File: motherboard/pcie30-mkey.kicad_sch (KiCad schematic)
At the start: 0 parts

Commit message: implemented most features
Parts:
- added C37, C38, C39, C40, C41, C42, C43, C44: 220nF, symbol Device:C_Small
- added C45, C46: 22uF, symbol Device:C_Small
- added C47, C57, C60, C62, C63: 1uF, symbol Device:C_Small
- added C48: 0.1uF, symbol Device:C_Small
- added C49: 100nF, Capacitor_SMD:C_0402_1005Metric, symbol Device:C_Small
- added C50: 10uF, Capacitor_SMD:C_1206_3216Metric, symbol Device:C_Small
- added C51: 1uF, Capacitor_SMD:C_1206_3216Metric, symbol Device:C_Small
- added C52: 22uF, Capacitor_SMD:C_0603_1608Metric, symbol Device:C_Small
- added C53: 8.2nF, Capacitor_SMD:C_0603_1608Metric, symbol Device:C_Small
- added C54: 1nF, Capacitor_SMD:C_0402_1005Metric, symbol Device:C_Small
- added C55: 10pF, Capacitor_SMD:C_0402_1005Metric, symbol Device:C_Small
- added C56, C61: 100nF, symbol Device:C_Small
- added C58, C59: 15pF, symbol Device:C_Small
- added D5: SS54, Diode_SMD:D_SMA, symbol Device:D_Schottky
- added IC1: PI6C557-05BLE, SOP65P640X120-20N:SOP65P640X120-20N, symbol PI6C557-05B:PI6C557-05BLE
- added J15: Bus_M.2_Socket_M, symbol Connector:Bus_M.2_Socket_M
- added L1: 3.3uH, Inductor_SMD:L_Vishay_IHLP-1616, symbol Device:L_Small
- added R63: 10k, Resistor_SMD:R_0402_1005Metric, symbol Device:R_Small
- added R64: 3.3k, Resistor_SMD:R_0402_1005Metric, symbol Device:R_Small
- added R65, R66: 13k, Resistor_SMD:R_0603_1608Metric, symbol Device:R_Small
- added R67: 4.7k, symbol Device:R_Small
- added R68, R69: NC, symbol Device:R_Small
- added R70, R71: 10k, symbol Device:R_Small
- added R72: 470R, symbol Device:R_Small
- added R73: 100R, symbol Device:R_Small
- added R74, R75, R78, R79, R82, R83: 33R, symbol Device:R_Small
- added R76, R77, R80, R81, R84, R85: 49.9R, symbol Device:R_Small
- added U20: TPS54331DR, TPS54331DR:SOIC127P599X175-8N, symbol TPS54331DR:TPS54331DR
- added U21: AP2127K-3.3, Package_TO_SOT_SMD:SOT-23-5, symbol Regulator_Linear:AP2127K-3.3
- added Y1: 25MHz, symbol Device:Crystal_GND24_Small
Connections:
- new net: R65.2, R66.1
- new net: C54.1, R66.2
- new net: C49.2, D5.1 (K), L1.2, U20.8 (PH)
- new net: IC1.8 (OE), R71.2
- new net: C59.1, R73.2, Y1.3
- new net: C38.2, J15.23 (PETn2)
- new net: R63.2, R64.1, U20.5 (VSENSE)
- new net: C39.2, J15.13 (PETp3)
- new net: C49.1, U20.1 (BOOT)
- new net: C53.1, U20.4 (SS)
- new net: C55.1, R65.1, U20.6 (COMP)
- new net: IC1.10 (IREF), R72.2
- new net: C42.2, J15.35 (PETn1)
- new net: C40.2, J15.25 (PETp2)
- new net: IC1.4 (S2), R67.2
- new net: IC1.3 (S1), R68.2
- new net: C43.2, J15.47 (PETn0/SATA-A-)
- new net: C41.2, J15.37 (PETp1)
- new net: C37.2, J15.11 (PETn3)
- new net: IC1.19 (~{CLK0}), R75.1
- new net: IC1.2 (S0), R69.2
- new net: IC1.20 (CLK0), R74.1
- new net: IC1.7 (~{PD}), R70.2
- new net: C44.2, J15.49 (PETp0/SATA-A+)
- new net +3.3V: U21.3 (EN)
- new net +3.3V_PCIE: C45.1, C46.1, C47.1, C48.1, C50.1, C51.1, J15.12 (3.3V), J15.14 (3.3V), J15.16 (3.3V), J15.18 (3.3V), J15.2 (3.3V), J15.4 (3.3V), J15.70 (3.3V), J15.72 (3.3V), J15.74 (3.3V), L1.1, R63.1
- new net +3.3V_PI6C: C56.1, C57.1, C60.1, C61.1, C63.1, IC1.1 (VDDXD), IC1.15 (VDDODA), R70.1, R71.1, U21.5 (VOUT)
- new net +5V: C62.1, U21.1 (VIN)
- new net +5v: C52.1, U20.2 (VIN)
- new net CLK2N: IC1.13 (~{CLK2}), R79.1
- new net CLK2P: IC1.14 (CLK2), R78.1
- new net CLK3N: IC1.11 (~{CLK3}), R83.1
- new net CLK3P: IC1.12 (CLK3), R82.1
- new net EN: U20.3 (EN)
- new net GND: C45.2, C46.2, C47.2, C48.2, C50.2, C51.2, C52.2, C53.2, C54.2, C55.2, C56.2, C57.2, C58.2, C59.2, C60.2, C61.2, C62.2, C63.2, D5.2 (A), IC1.16 (GNDODA), IC1.9 (GNDXD), J15.1 (GND), J15.15 (GND), J15.21 (GND), J15.27 (GND), J15.3 (GND), J15.33 (GND), J15.39 (GND), J15.45 (GND), J15.51 (GND), J15.57 (GND), J15.71 (GND), J15.73 (GND), J15.75 (GND), J15.9 (GND), R64.2, R67.1, R68.1, R69.1, R72.1, R76.1, R77.1, R80.1, R81.1, R84.1, R85.1, U20.7 (GND), U21.2 (GND), Y1.2, Y1.4
- new net GPIO4_B4/PCIE30X4_CLKREQn_M1_L: J15.52 (~{CLKREQ})
- new net GPIO4_B5/PCIE30X4_WAKEn_M1_L: J15.54 (~{PEWAKE})
- new net GPIO4_B6/PCIE30X4_PERSTn_M1_L: J15.50 (~{PERST})
- new net PCIE30_PORT0_REFCLKN_IN: R83.2, R85.2
- new net PCIE30_PORT0_REFCLKP_IN: R82.2, R84.2
- new net PCIE30_PORT0_RX0N: J15.41 (PERn0/SATA-B+)
- new net PCIE30_PORT0_RX0P: J15.43 (PERp0/SATA-B-)
- new net PCIE30_PORT0_RX1N: J15.29 (PERn1)
- new net PCIE30_PORT0_RX1P: J15.31 (PERp1)
- new net PCIE30_PORT0_TX0N: C43.1
- new net PCIE30_PORT0_TX0P: C44.1
- new net PCIE30_PORT0_TX1N: C42.1
- new net PCIE30_PORT0_TX1P: C41.1
- new net PCIE30_PORT1_RX2N: J15.17 (PERn2)
- new net PCIE30_PORT1_RX2P: J15.19 (PERp2)
- new net PCIE30_PORT1_RX3N: J15.5 (PERn3)
- new net PCIE30_PORT1_RX3P: J15.7 (PERp3)
- new net PCIE30_PORT1_TX2N: C38.1
- new net PCIE30_PORT1_TX2P: C40.1
- new net PCIE30_PORT1_TX3N: C37.1
- new net PCIE30_PORT1_TX3P: C39.1
- new net PCIE30_REFCLKN_SLOT: J15.53 (REFCLKn)
- new net PCIE30_REFCLKP_SLOT: J15.55 (REFCLKp)
- new net PCIE30_REFCLK_A_N: R75.2, R77.2
- new net PCIE30_REFCLK_A_P: R74.2, R76.2
- new net PCIE30_REFCLK_B_N: R79.2, R81.2
- new net PCIE30_REFCLK_B_P: R78.2, R80.2
- new net X1: C58.1, IC1.5 (X1), Y1.1
- new net X2: IC1.6 (X2), R73.1
- no-connect marks 0 -> 6
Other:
- note added: "internal pull up"

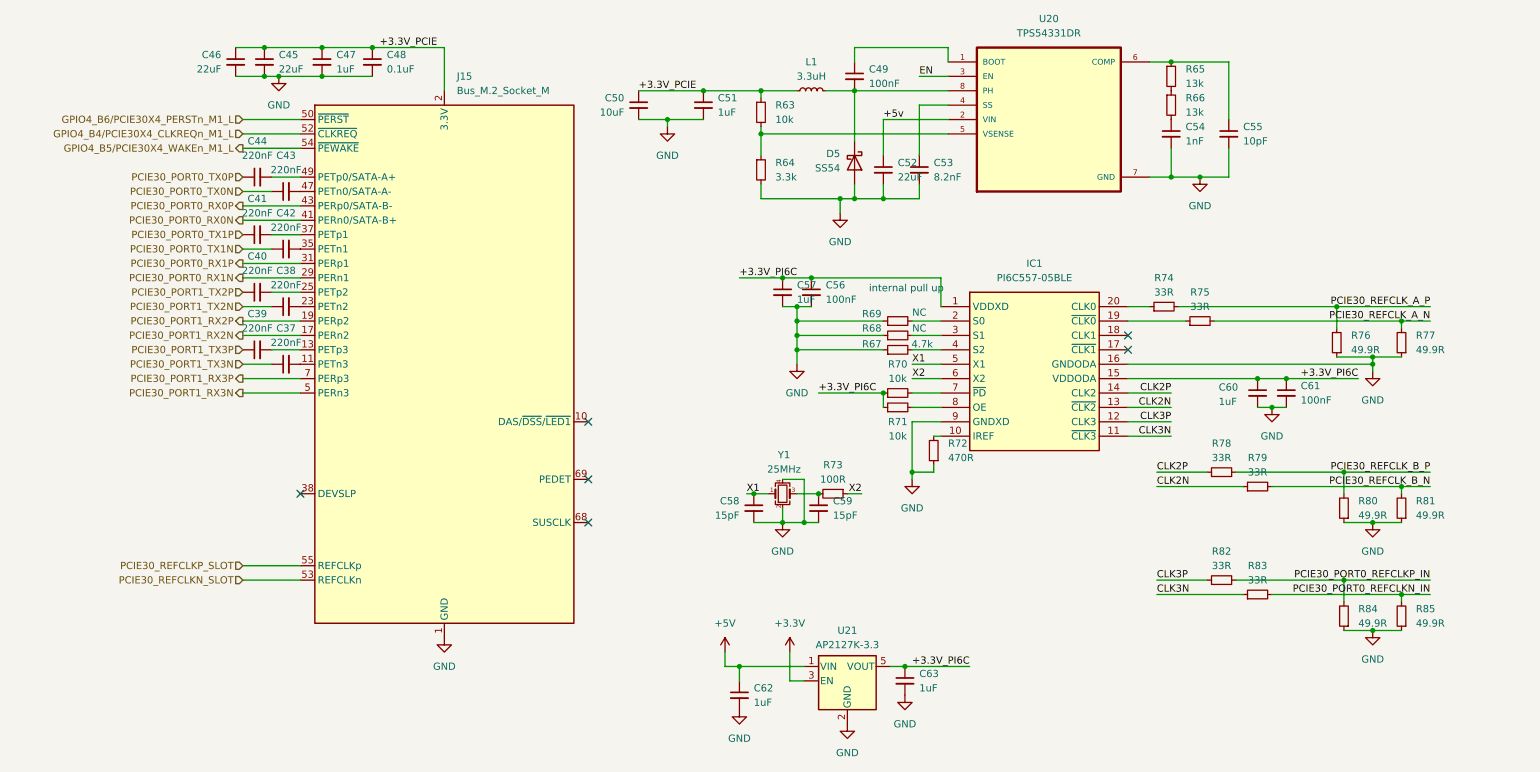
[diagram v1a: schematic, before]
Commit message: synchronizing hierarchical pins
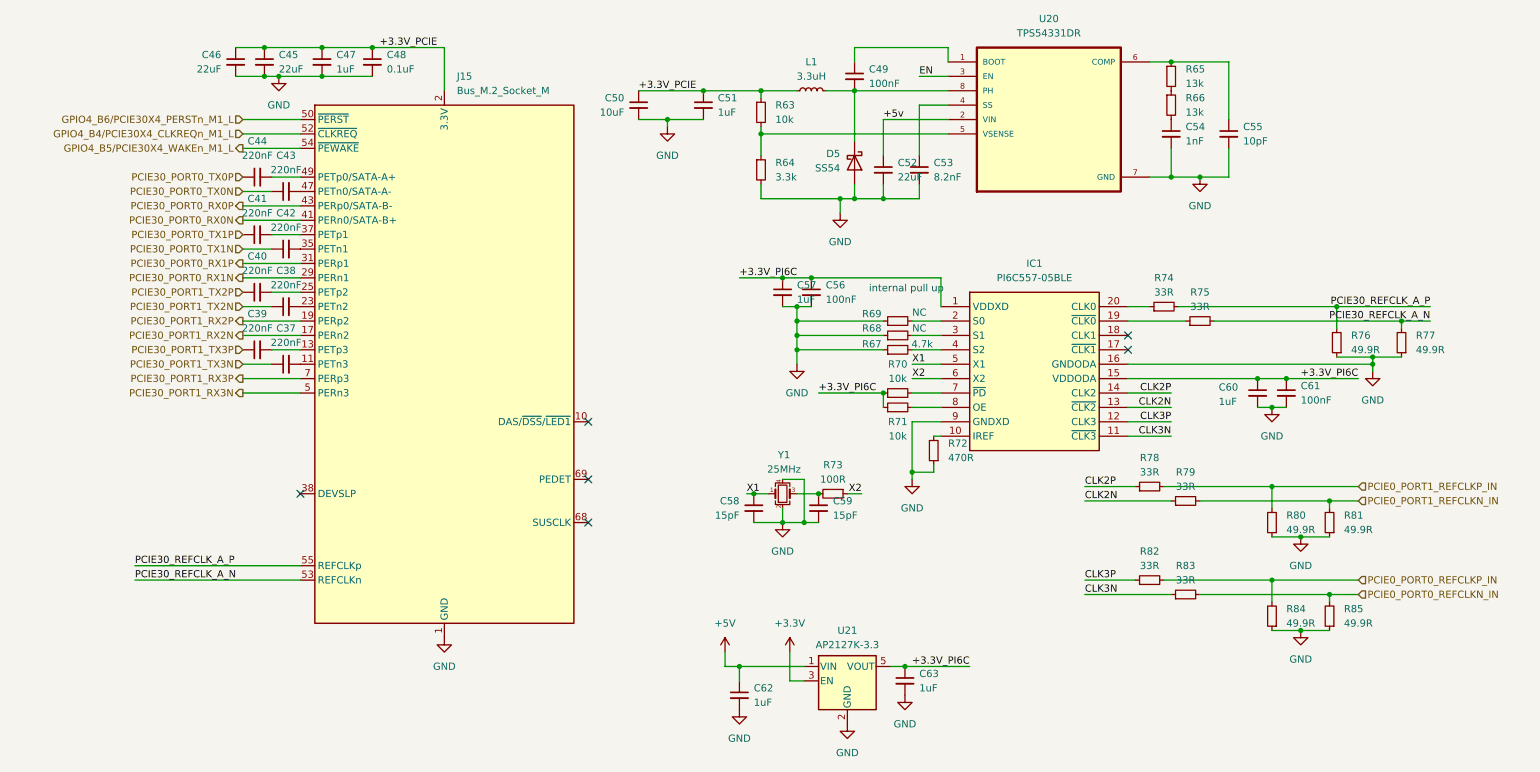
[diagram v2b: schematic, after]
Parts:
- C37, C38, C39, C40, C41, C42, C43, C44, C45, C46, C47, C48, C56, C57, C58, C59, C60, C61, C62, C63: footprint (none) -> Capacitor_SMD:C_0402_1005Metric
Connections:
- net PCIE30_REFCLKN_SLOT is gone; now on net PCIE30_REFCLK_A_N: J15.53 (REFCLKn)
- net PCIE30_REFCLKP_SLOT is gone; now on net PCIE30_REFCLK_A_P: J15.55 (REFCLKp)
- net PCIE30_PORT0_REFCLKN_IN renamed PCIE0_PORT0_REFCLKN_IN
- net PCIE30_PORT0_REFCLKP_IN renamed PCIE0_PORT0_REFCLKP_IN
- net PCIE30_REFCLK_B_N renamed PCIE0_PORT1_REFCLKN_IN
- net PCIE30_REFCLK_B_P renamed PCIE0_PORT1_REFCLKP_IN
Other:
- moved on the sheet: R78, R79, R80, R81, R82, R83, R84, R85

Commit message: linked all footprints
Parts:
- J15: footprint (none) -> NVME_M_KEY:CONN-SMD_AS0BC21-S30BM-7H
- R65, R66: footprint Resistor_SMD:R_0603_1608Metric -> Resistor_SMD:R_0402_1005Metric
- R67, R68, R69, R70, R71, R72, R73, R74, R75, R76, R77, R78, R79, R80, R81, R82, R83, R84, R85: footprint (none) -> Resistor_SMD:R_0402_1005Metric
- Y1: footprint (none) -> Crystal:Crystal_SMD_2016-4Pin_2.0x1.6mm
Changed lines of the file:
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@@
 			)
 		)
-		(property "Footprint" "Resistor_SMD:R_0603_1608Metric"
+		(property "Footprint" "Resistor_SMD:R_0402_1005Metric"
 			(at 215.9 30.48 0)
 			(effects
@@
 			)
 		)
-		(property "Footprint" ""
+		(property "Footprint" "Resistor_SMD:R_0402_1005Metric"
 			(at 212.09 97.79 0)
 			(effects
@@
 			)
 		)
-		(property "Footprint" ""
+		(property "Footprint" "Resistor_SMD:R_0402_1005Metric"
 			(at 167.64 83.82 0)
 			(effects
@@
 			)
 		)
-		(property "Footprint" ""
+		(property "Footprint" "Crystal:Crystal_SMD_2016-4Pin_2.0x1.6mm"
 			(at 147.32 99.06 0)
 			(effects
@@
 			)
 		)
-		(property "Footprint" ""
+		(property "Footprint" "Resistor_SMD:R_0402_1005Metric"
 			(at 256.54 72.39 0)
 			(effects
@@
 			)
 		)
-		(property "Footprint" ""
+		(property "Footprint" "Resistor_SMD:R_0402_1005Metric"
 			(at 233.68 104.14 0)
 			(effects
@@
 			)
 		)
-		(property "Footprint" ""
+		(property "Footprint" "Resistor_SMD:R_0402_1005Metric"
 			(at 173.99 91.44 0)
 			(effects
@@
 			)
 		)
-		(property "Footprint" ""
+		(property "Footprint" "Resistor_SMD:R_0402_1005Metric"
 			(at 167.64 73.66 0)
 			(effects
@@
 			)
 		)
-		(property "Footprint" ""
+		(property "Footprint" "Resistor_SMD:R_0402_1005Metric"
 			(at 167.64 71.12 0)
 			(effects
@@
 			)
 		)
-		(property "Footprint" ""
+		(property "Footprint" "Resistor_SMD:R_0402_1005Metric"
 			(at 233.68 120.65 0)
 			(effects
@@
 			)
 		)
-		(property "Footprint" ""
+		(property "Footprint" "Resistor_SMD:R_0402_1005Metric"
 			(at 218.44 116.84 0)
 			(effects
@@
 			)
 		)
-		(property "Footprint" "Resistor_SMD:R_0603_1608Metric"
+		(property "Footprint" "Resistor_SMD:R_0402_1005Metric"
 			(at 215.9 25.4 0)
 			(effects
@@
 			)
 		)
-		(property "Footprint" ""
+		(property "Footprint" "Resistor_SMD:R_0402_1005Metric"
 			(at 218.44 100.33 0)
 			(effects
@@
 			)
 		)
-		(property "Footprint" ""
+		(property "Footprint" "Resistor_SMD:R_0402_1005Metric"
 			(at 212.09 114.3 0)
 			(effects
@@
 			)
 		)
-		(property "Footprint" ""
+		(property "Footprint" "NVME_M_KEY:CONN-SMD_AS0BC21-S30BM-7H"
 			(at 87.63 49.53 0)
 			(effects
@@
 			)
 		)
-		(property "Footprint" ""
+		(property "Footprint" "Resistor_SMD:R_0402_1005Metric"
 			(at 167.64 68.58 0)
 			(effects
@@
 			)
 		)
-		(property "Footprint" ""
+		(property "Footprint" "Resistor_SMD:R_0402_1005Metric"
 			(at 220.98 68.58 0)
 			(effects
@@
 			)
 		)
-		(property "Footprint" ""
+		(property "Footprint" "Resistor_SMD:R_0402_1005Metric"
 			(at 167.64 81.28 0)
 			(effects
@@
 			)
 		)
-		(property "Footprint" ""
+		(property "Footprint" "Resistor_SMD:R_0402_1005Metric"
 			(at 214.63 66.04 0)
 			(effects
@@
 			)
 		)
-		(property "Footprint" ""
+		(property "Footprint" "Resistor_SMD:R_0402_1005Metric"
 			(at 243.84 120.65 0)
 			(effects
@@
 			)
 		)
-		(property "Footprint" ""
+		(property "Footprint" "Resistor_SMD:R_0402_1005Metric"
 			(at 243.84 104.14 0)
 			(effects
@@
 			)
 		)
-		(property "Footprint" ""
+		(property "Footprint" "Resistor_SMD:R_0402_1005Metric"
 			(at 245.11 72.39 0)
 			(effects
@@
 			)
 		)
-		(property "Footprint" ""
+		(property "Footprint" "Resistor_SMD:R_0402_1005Metric"
 			(at 156.21 99.06 0)
 			(effects
